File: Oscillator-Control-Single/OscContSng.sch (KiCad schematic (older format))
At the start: 61 parts, among them J1 CortexM_Debug, J3 USB_OTG, SW1 Waveform, SW11 Release, SW4 Attack, SW5 Decay, SW9 Sustain, U1 AZ1117-3.3, U2 SAMD20E15A/B-A, Y1 32.768kHz

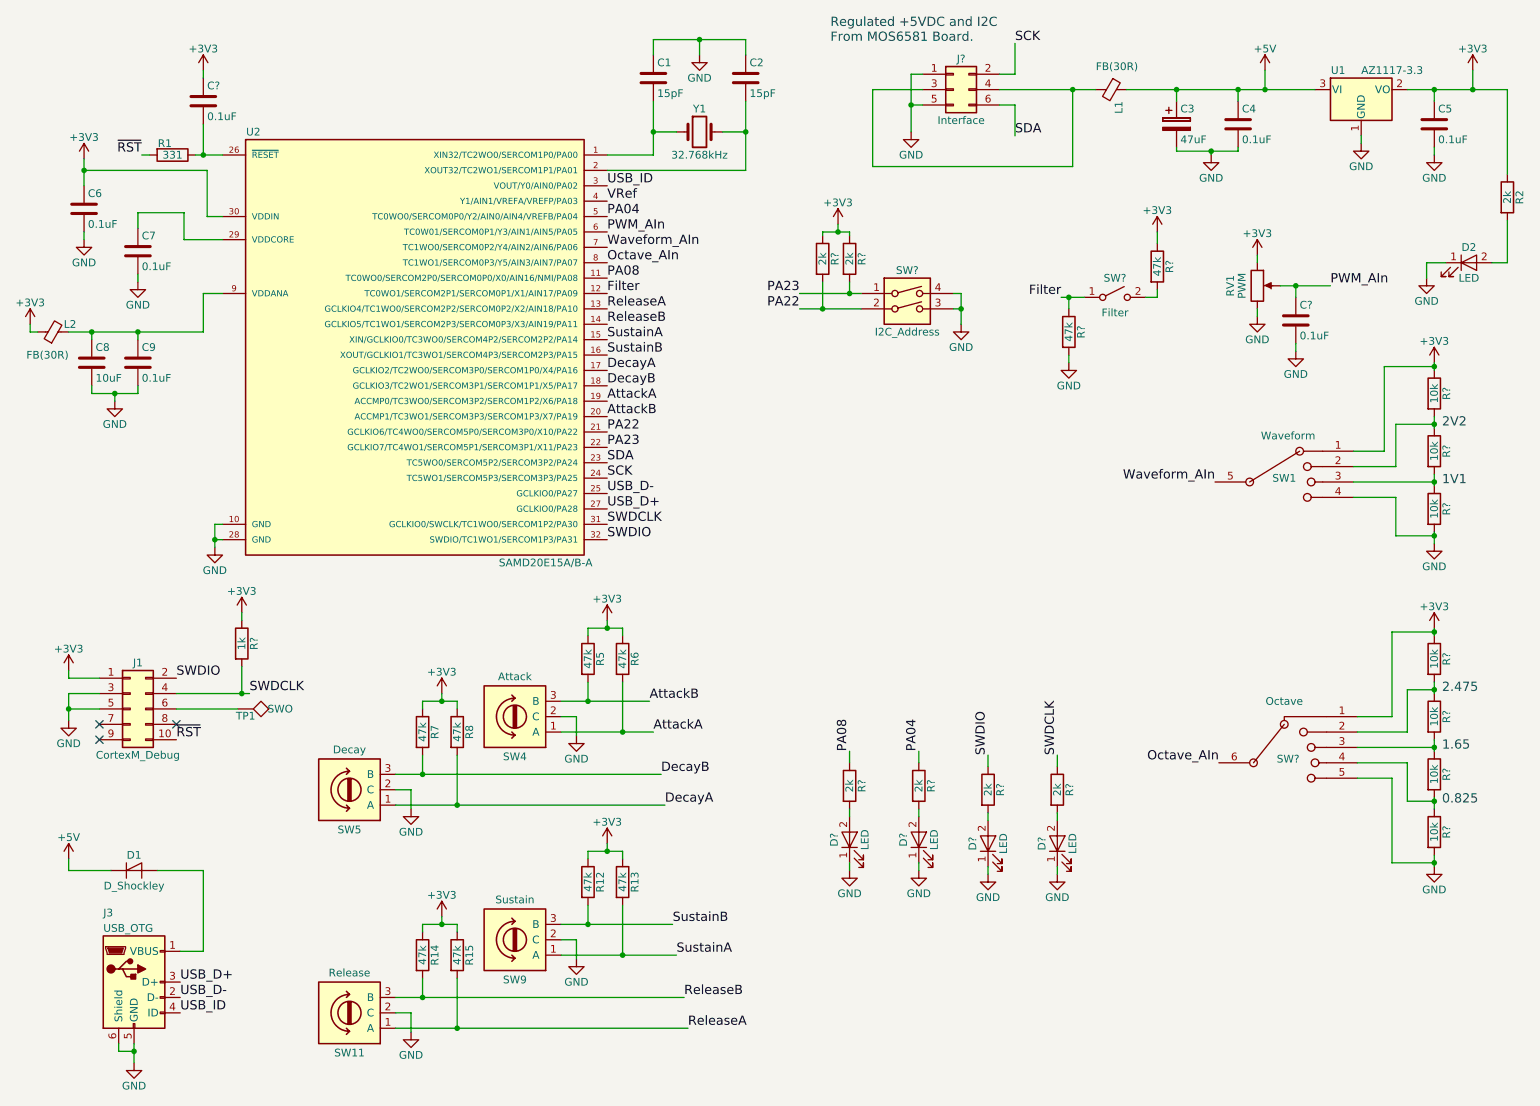
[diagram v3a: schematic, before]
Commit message: added footprints.
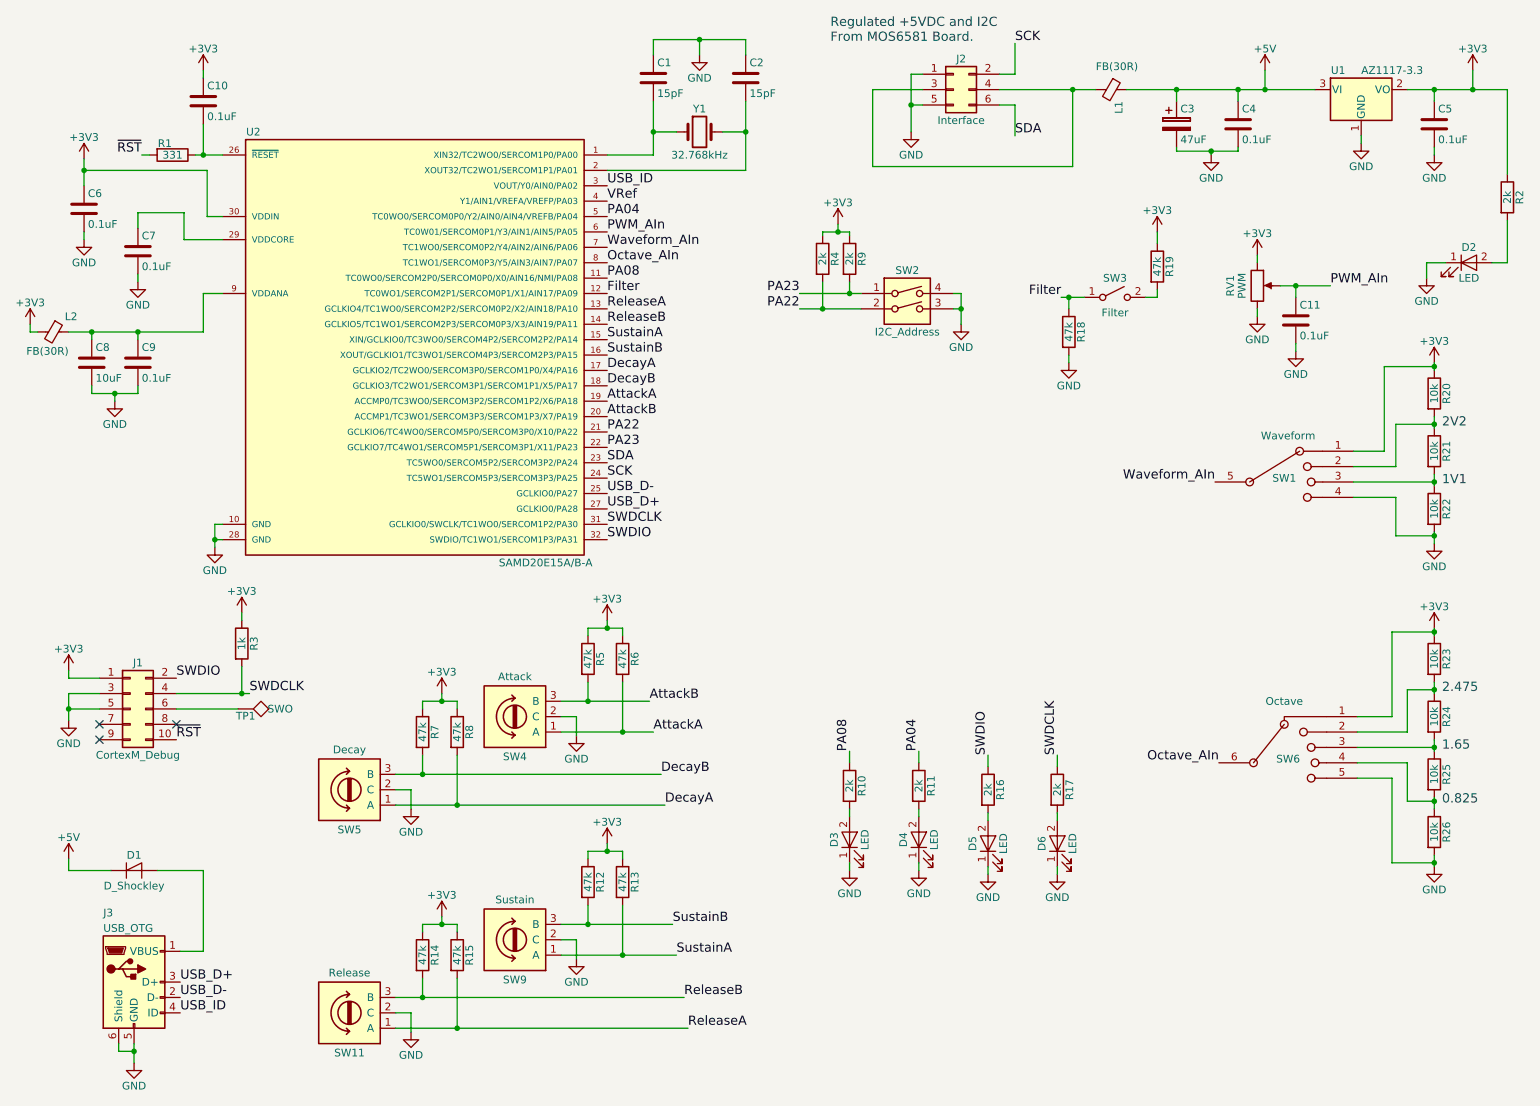
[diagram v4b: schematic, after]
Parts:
- C1, C2, C4, C5, C6, C7, C9: footprint (none) -> Capacitors_SMD:C_0603_HandSoldering
- C10, C11: renamed from C?; footprint (none) -> Capacitors_SMD:C_0603_HandSoldering
- C8: footprint (none) -> Capacitors_SMD:C_0805_HandSoldering
- D1: footprint (none) -> Resistors_SMD:R_0805_HandSoldering
- D2, R1, R12, R13, R14, R15, R2, R5, R6, R7, R8: footprint (none) -> Resistors_SMD:R_0603_HandSoldering
- L2: footprint (none) -> Resistors_SMD:R_0805_HandSoldering; Critical (none) -> N; Description (none) -> FERRITE BEAD 30 OHM 0805 1LN; Source (none) -> 1276-6370-1-ND; VPN (none) -> CIS21P300NE
- R10, R11, R16, R17, R18, R19, R20, R21, R22, R23, R24, R25, R26, R3, R4, R9: renamed from R?; footprint (none) -> Resistors_SMD:R_0603_HandSoldering
- gave numbers to parts that had none: 8
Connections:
- net +3V3: now also L2.2; no longer L2.1
- net at C8.1, C9.1, U2.9 (VDDANA): now also L2.1; no longer L2.2
